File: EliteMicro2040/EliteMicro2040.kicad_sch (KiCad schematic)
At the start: 40 parts, among them J2 Button, J5 Conn_01x03_Male, U101 TLV70033, U2 Elite-C, U3 RP2040, Y1 2520_4P 12Mhz

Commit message: preparation for order.
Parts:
- removed J5: Conn_01x03_Male, Connector_PinHeader_2.54mm:PinHeader_1x03_P2.54mm_Vertical, symbol Connector_Generic:Conn_01x03
- added TP101, TP102, TP103: TestPoint, EnvExtras:CustomTestPoint, symbol Connector:TestPoint
- FLASH1: value W25Q16FWUXIE -> W25Q16JVUXIQ
- USB1: LCSC C165948 -> C223907
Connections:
- net GND: now also TP102.1
- net SWCLK: now also TP101.1
- net SWD: now also TP103.1
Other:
- note removed: "D1 NEEDS to be 0omh resistor or 1N4002 diode"
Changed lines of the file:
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@@
     (effects (font (size 1.27 1.27)) (justify right bottom))
-  )
-  (text "D1 NEEDS to be 0omh resistor or 1N4002 diode" (at 70.485 47.625 0)
-    (effects (font (size 0.508 0.508)) (justify left bottom))
   )
   (text "Im pretty sure a lot of these W25QXXX Chips are pin compatible\nDont quote me on that"
@@
       (effects (font (size 1.27 1.27)) hide)
     )
-    (property "LCSC" "C165948" (id 4) (at 25.4 35.56 0)
+    (property "LCSC" "C223907" (id 4) (at 25.4 35.56 0)
       (effects (font (size 1.27 1.27)) hide)
     )
@@
     (in_bom yes) (on_board yes)
     (property "Reference" "FLASH1" (id 0) (at 78.74 133.35 0))
-    (property "Value" "W25Q16FWUXIE" (id 1) (at 78.74 146.05 0))
+    (property "Value" "W25Q16JVUXIQ" (id 1) (at 78.74 146.05 0))
     (property "Footprint" "Package_SON:SON-8-1EP_3x2mm_P0.5mm_EP1.4x1.6mm" (id 2) (at 78.74 133.35 0)
       (effects (font (size 1.27 1.27)) (justify left bottom) hide)
@@
     )
     (pin "1")
-  )
-  (symbol (lib_id "Connector_Generic:Conn_01x03") (at 375.92 177.8 0) (unit 1)
-    (in_bom yes) (on_board yes)
-    (property "Reference" "J5" (id 0) (at 377.952 176.7332 0)
-      (effects (font (size 1.27 1.27)) (justify left))
-    )
-    (property "Value" "Conn_01x03_Male" (id 1) (at 377.952 179.0446 0)
-      (effects (font (size 1.27 1.27)) (justify left))
-    )
-    (property "Footprint" "Connector_PinHeader_2.54mm:PinHeader_1x03_P2.54mm_Vertical" (id 2) (at 375.92 177.8 0)
-      (effects (font (size 1.27 1.27)) hide)
-    )
-    (property "Datasheet" "" (id 3) (at 375.92 177.8 0)
-      (effects (font (size 1.27 1.27)) hide)
-    )
-    (property "LCSC" " " (id 4) (at 375.92 177.8 0)
-      (effects (font (size 1.27 1.27)) hide)
-    )
-    (pin "1")
-    (pin "2")
-    (pin "3")
   )
   (symbol (lib_id "power:GND") (at 370.84 177.8 270) (unit 1)
@@
     (pin "1")
   )
+  (symbol (lib_id "Connector:TestPoint") (at 370.84 177.8 270) (unit 1)
+    (in_bom yes) (on_board yes)
+    (property "Reference" "TP102" (id 0) (at 375.6152 177.2412 90)
+      (effects (font (size 0.508 0.508)) (justify left))
+    )
+    (property "Value" "TestPoint" (id 1) (at 375.6152 178.3334 90)
+      (effects (font (size 0.508 0.508)) (justify left))
+    )
+    (property "Footprint" "EnvExtras:CustomTestPoint" (id 2) (at 370.84 182.88 0)
+      (effects (font (size 1.27 1.27)) hide)
+    )
+    (property "Datasheet" "" (id 3) (at 370.84 182.88 0)
+      (effects (font (size 1.27 1.27)) hide)
+    )
+    (property "LCSC" " " (id 4) (at 370.84 177.8 0)
+      (effects (font (size 1.27 1.27)) hide)
+    )
+    (pin "1")
+  )
   (symbol (lib_id "power:GND") (at 68.58 57.15 0) (unit 1)
     (in_bom yes) (on_board yes)
@@
     (pin "1")
     (pin "2")
+  )
+  (symbol (lib_id "Connector:TestPoint") (at 370.84 175.26 270) (unit 1)
+    (in_bom yes) (on_board yes)
+    (property "Reference" "TP101" (id 0) (at 375.6152 174.7012 90)
+      (effects (font (size 0.508 0.508)) (justify left))
+    )
+    (property "Value" "TestPoint" (id 1) (at 375.6152 175.7934 90)
+      (effects (font (size 0.508 0.508)) (justify left))
+    )
+    (property "Footprint" "EnvExtras:CustomTestPoint" (id 2) (at 370.84 180.34 0)
+      (effects (font (size 1.27 1.27)) hide)
+    )
+    (property "Datasheet" "" (id 3) (at 370.84 180.34 0)
+      (effects (font (size 1.27 1.27)) hide)
+    )
+    (property "LCSC" " " (id 4) (at 370.84 175.26 0)
+      (effects (font (size 1.27 1.27)) hide)
+    )
+    (pin "1")
+  )
+  (symbol (lib_id "Connector:TestPoint") (at 370.84 180.34 270) (unit 1)
+    (in_bom yes) (on_board yes)
+    (property "Reference" "TP103" (id 0) (at 375.6152 179.7812 90)
+      (effects (font (size 0.508 0.508)) (justify left))
+    )
+    (property "Value" "TestPoint" (id 1) (at 375.6152 180.8734 90)
+      (effects (font (size 0.508 0.508)) (justify left))
+    )
+    (property "Footprint" "EnvExtras:CustomTestPoint" (id 2) (at 370.84 185.42 0)
+      (effects (font (size 1.27 1.27)) hide)
+    )
+    (property "Datasheet" "" (id 3) (at 370.84 185.42 0)
+      (effects (font (size 1.27 1.27)) hide)
+    )
+    (property "LCSC" " " (id 4) (at 370.84 180.34 0)
+      (effects (font (size 1.27 1.27)) hide)
+    )
+    (pin "1")
   )
   (sheet_instances
@@
     )
     (path "/00000000-0000-0000-0000-0000608edada"
-      (reference "FLASH1") (unit 1) (value "W25Q16FWUXIE") (footprint "Package_SON:SON-8-1EP_3x2mm_P0.5mm_EP1.4x1.6mm")
+      (reference "FLASH1") (unit 1) (value "W25Q16JVUXIQ") (footprint "Package_SON:SON-8-1EP_3x2mm_P0.5mm_EP1.4x1.6mm")
     )
     (path "/00000000-0000-0000-0000-000060cc7b32"
@@
       (reference "J2") (unit 1) (value "Button") (footprint "Button_Switch_SMD:SW_SPST_CK_KXT3")
     )
-    (path "/00000000-0000-0000-0000-000060ce2dd4"
-      (reference "J5") (unit 1) (value "Conn_01x03_Male") (footprint "Connector_PinHeader_2.54mm:PinHeader_1x03_P2.54mm_Vertical")
-    )
     (path "/00000000-0000-0000-0000-00005edae9f0"
       (reference "R1") (unit 1) (value "1K 402 Resistor") (footprint "Capacitor_SMD:C_0402_1005Metric")
@@
       (reference "TP4") (unit 1) (value "TestPoint") (footprint "EnvExtras:CustomTestPoint")
     )
+    (path "/cc629fb9-56a0-47df-8b5b-822906a0848a"
+      (reference "TP101") (unit 1) (value "TestPoint") (footprint "EnvExtras:CustomTestPoint")
+    )
+    (path "/42a77294-7232-471b-9aeb-b80d6a159af4"
+      (reference "TP102") (unit 1) (value "TestPoint") (footprint "EnvExtras:CustomTestPoint")
+    )
+    (path "/e62dbc5e-8e6b-40c9-9254-b5ec34005539"
+      (reference "TP103") (unit 1) (value "TestPoint") (footprint "EnvExtras:CustomTestPoint")
+    )
     (path "/00000000-0000-0000-0000-000061b490e3"

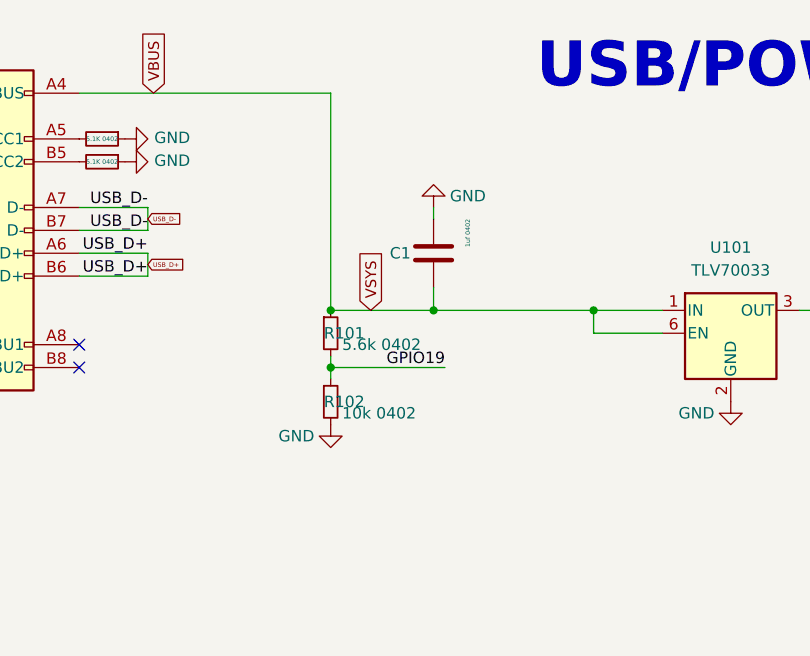
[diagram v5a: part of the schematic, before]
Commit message: added diode after VBUS to make sure VBUS Detect can work properly.
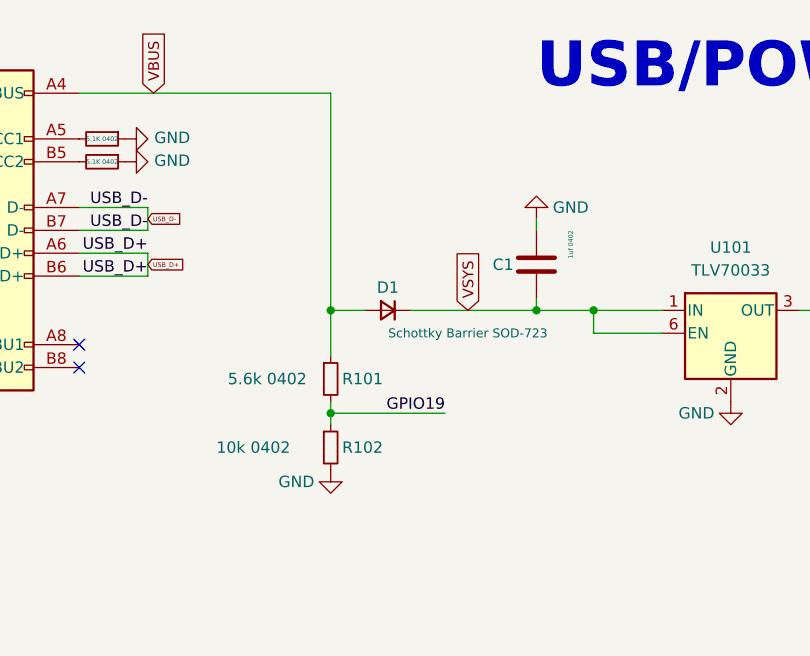
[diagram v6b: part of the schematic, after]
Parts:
- added D1: Schottky Barrier SOD-723, Diode_SMD:D_SOD-523, symbol Device:D_Small
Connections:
- net VBUS: now also D1.2 (A); no longer C1.1, U101.1 (IN), U101.6 (EN)
- new net VSYS: C1.1, D1.1 (K), U101.1 (IN), U101.6 (EN)
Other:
- moved on the sheet: C1, R101, R102

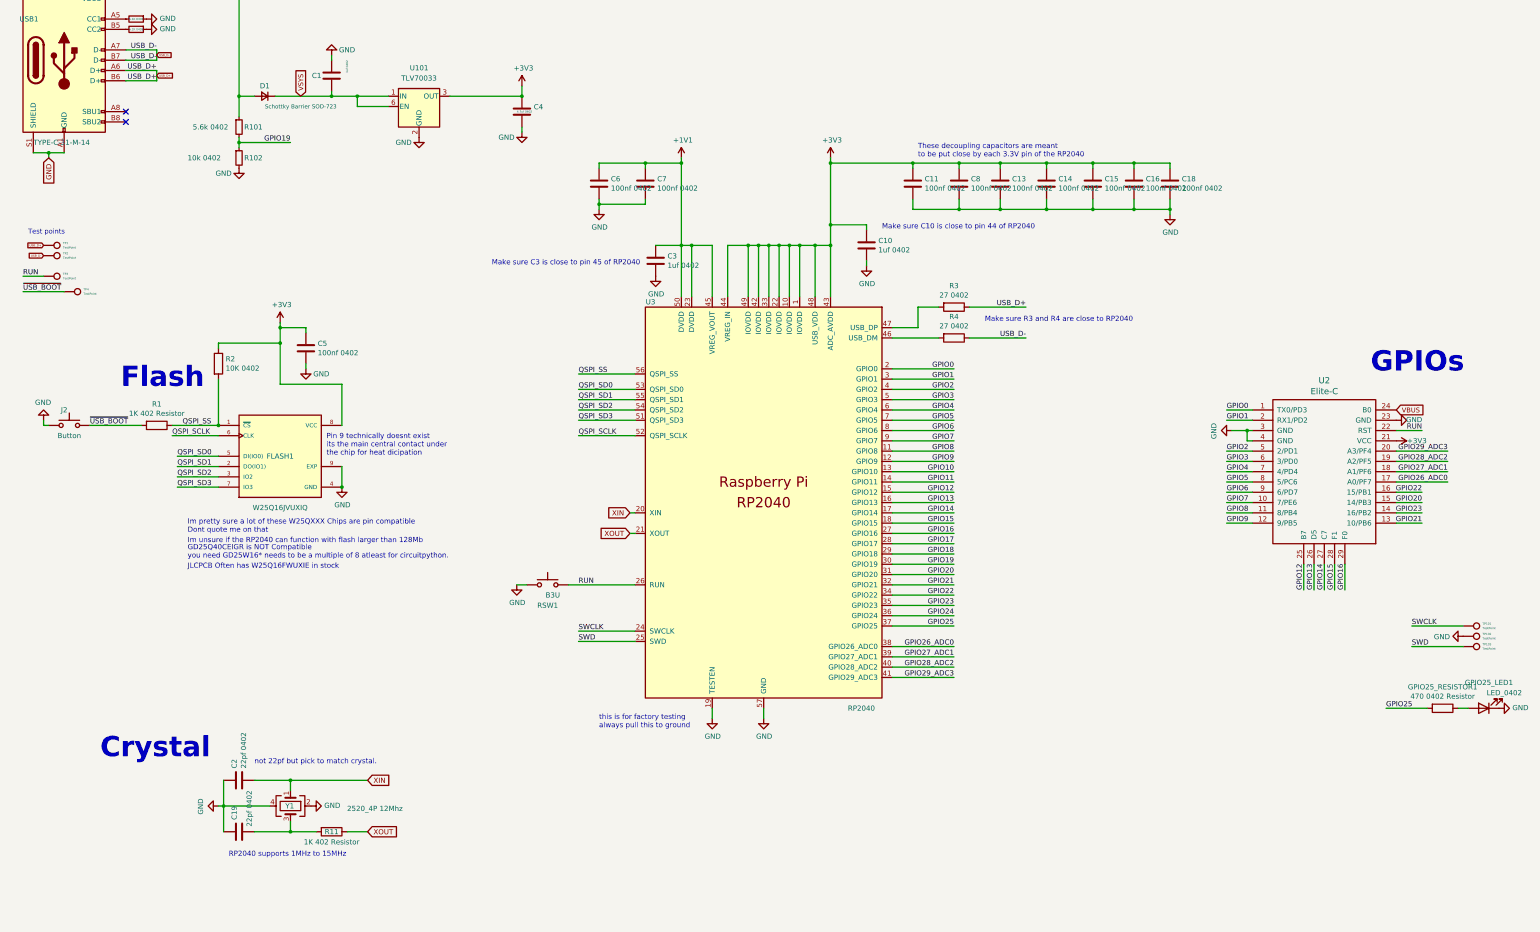
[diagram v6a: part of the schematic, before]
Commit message: made various improvements to design such as swapping vbus for vsys on the raw pin
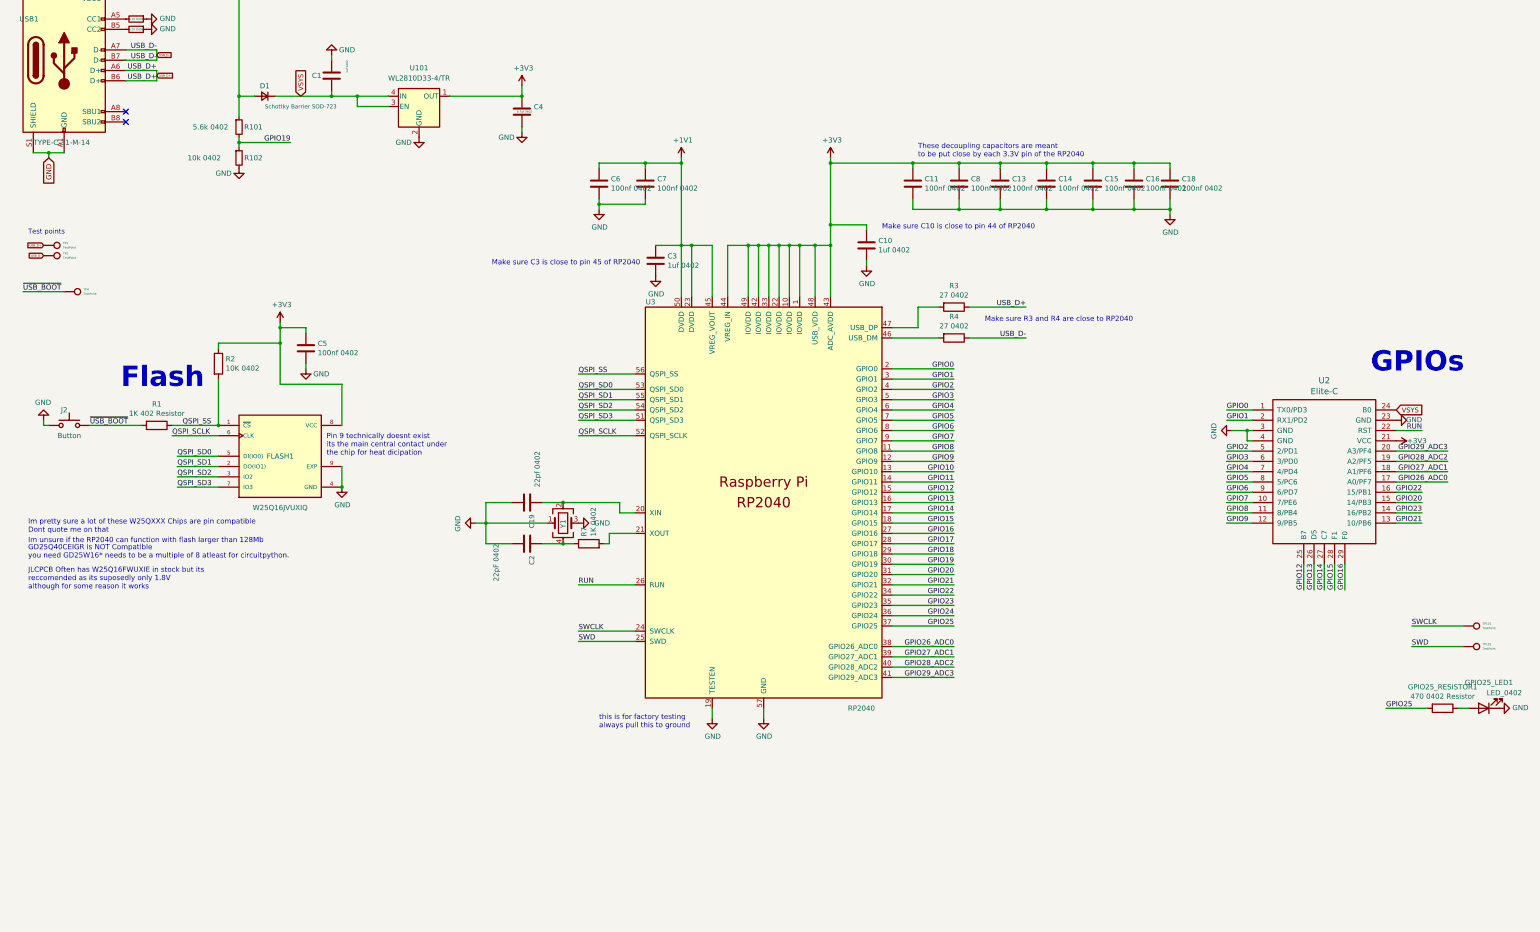
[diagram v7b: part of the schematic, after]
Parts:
- removed R11: 1K 402 Resistor, Capacitor_SMD:C_0402_1005Metric, symbol Device:R
- removed RSW1: B3U, Button_Switch_SMD:SW_SPST_B3U-1000P, symbol Switch:SW_Push
- removed TP102, TP3: TestPoint, EnvExtras:CustomTestPoint, symbol Connector:TestPoint
- added R7: 1K 0402, Capacitor_SMD:C_0402_1005Metric, symbol Device:R
- C2: value 22pf 0402 -> 22pF 0402
- U101: value TLV70033 -> WL2810D33-4/TR; footprint Package_SON:WSON-6_1.5x1.5mm_P0.5mm -> Package_DFN_QFN:UDFN-4-1EP_1x1mm_P0.65mm_EP0.48x0.48mm
- Y1: value 2520_4P 12Mhz -> 2016_4P; footprint Crystal:Crystal_SMD_2520-4Pin_2.5x2.0mm -> Crystal:Crystal_SMD_2016-4Pin_2.0x1.6mm
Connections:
- net +3V3: now also U101.1 (OUT); no longer U101.3 (OUT)
- net GND: now also C19.2, C2.2, Y1.1, Y1.3; no longer C19.1, C2.1, Y1.2, Y1.4
- net VBUS: no longer U2.24 (B0)
- net VSYS: now also U101.3 (EN), U101.4 (NC), U2.24 (B0); no longer U101.1 (IN), U101.6 (EN)
- removed net XIN: C2.2, U3.20 (XIN), Y1.1
- net XOUT: no longer names the net of U3.21 (XOUT)
- net XOUT: now also R7.2
- new net: C19.1, U3.20 (XIN), Y1.2
- new net: C2.1, R7.1, Y1.4
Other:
- note added: "JLCPCB Often has W25Q16FWUXIE in stock but its reccomended as its suposedly only 1.8V although for some reason it works"
- note removed: "Crystal"
- note removed: "JLCPCB Often has W25Q16FWUXIE in stock"
- note removed: "RP2040 supports 1MHz to 15MHz"
- note removed: "not 22pf but pick to match crystal."
- moved on the sheet: C19, C2, Y1

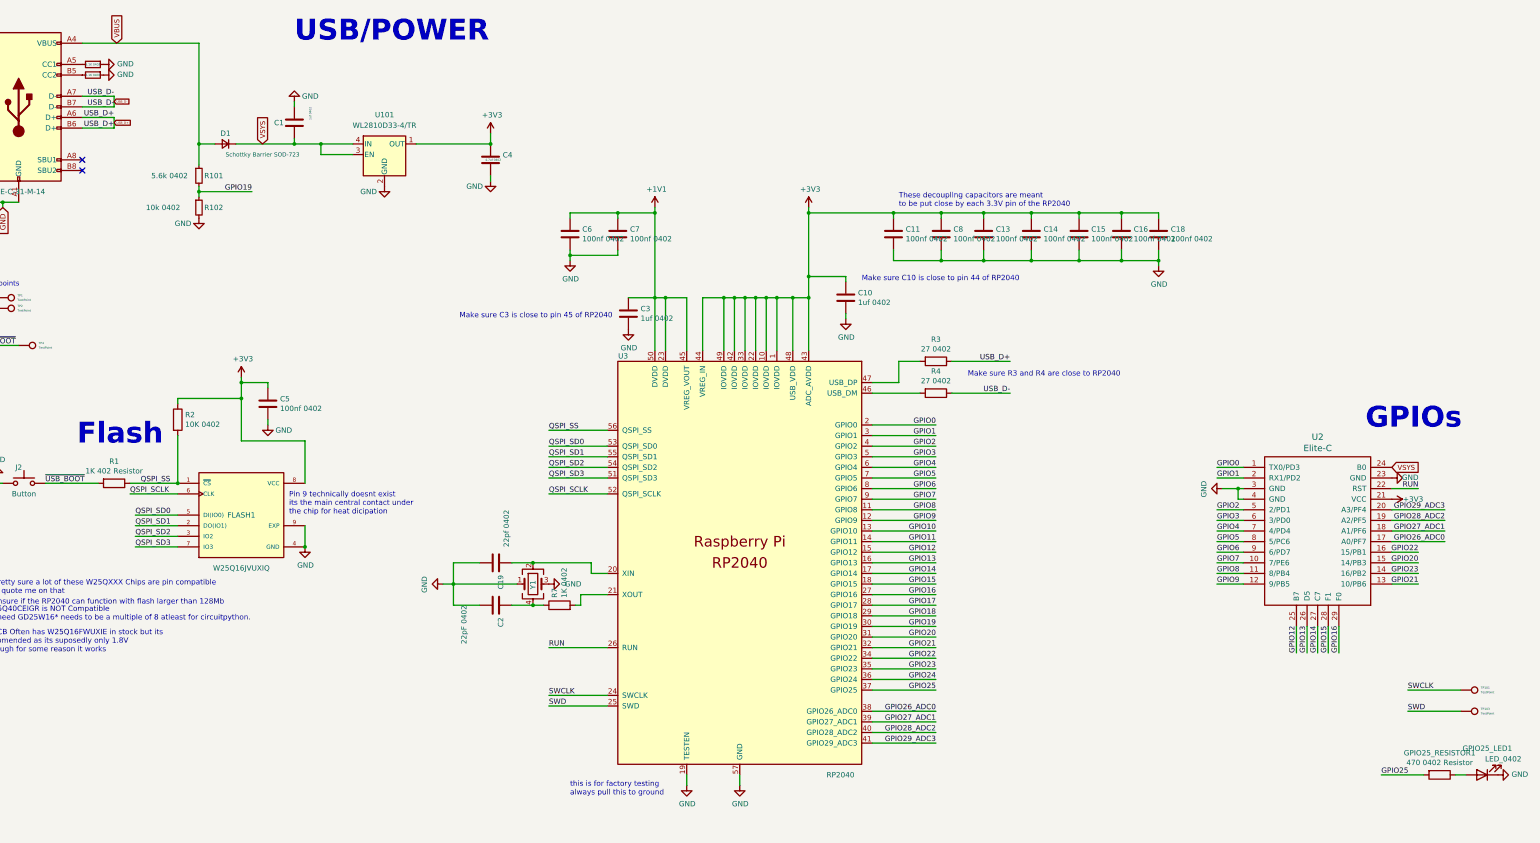
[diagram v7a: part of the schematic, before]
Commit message: General re-work of board to ensure less chance of failure
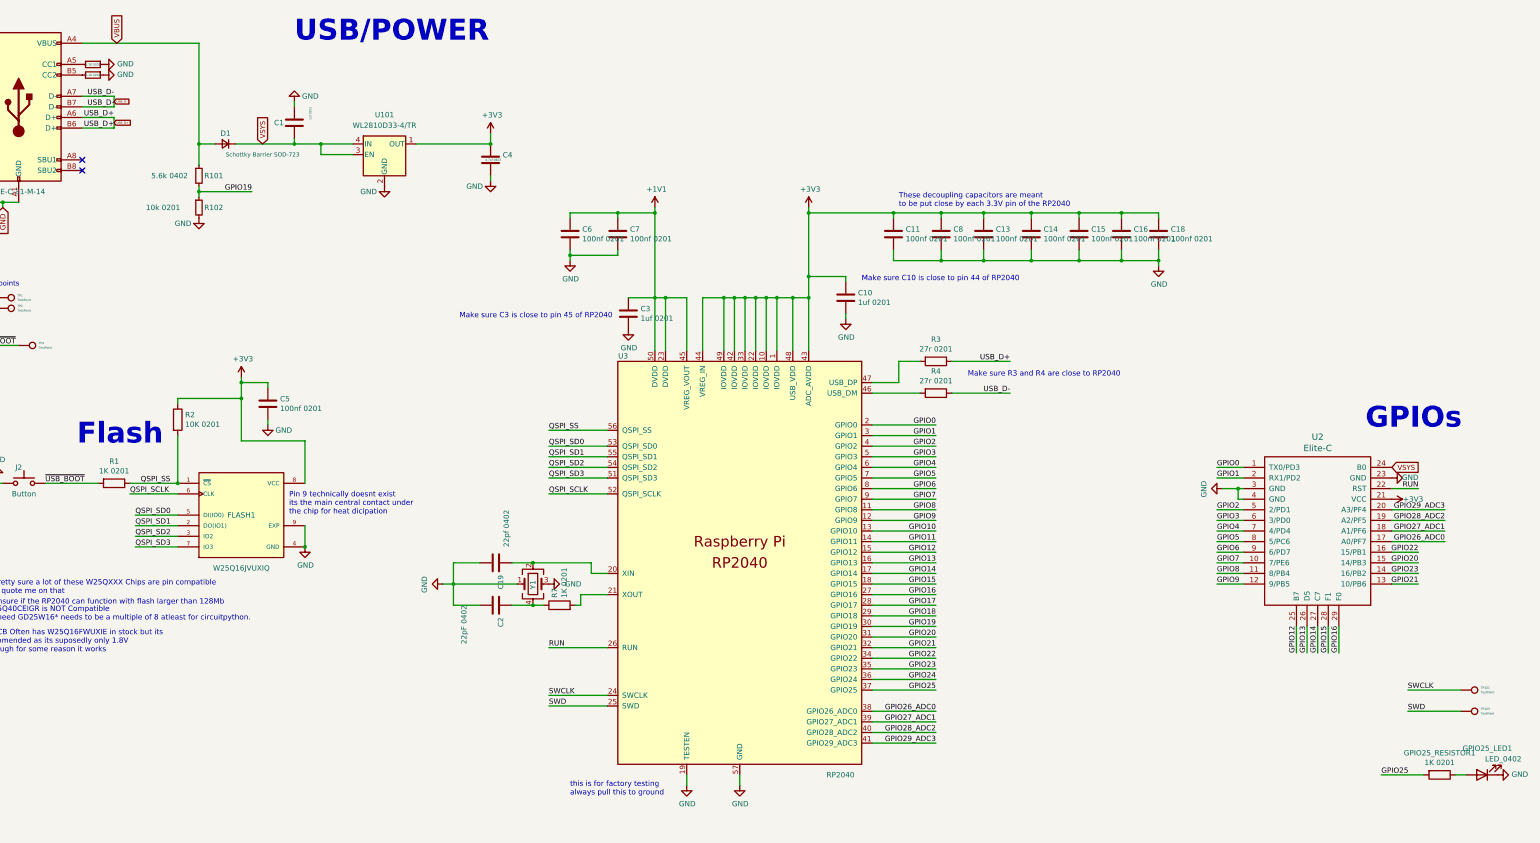
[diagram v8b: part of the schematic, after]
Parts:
- C1, C10, C3: value 1uf 0402 -> 1uf 0201; footprint Capacitor_SMD:C_0402_1005Metric -> Capacitor_SMD:C_0201_0603Metric
- C11, C13, C14, C15, C16, C18, C5, C6, C7, C8: value 100nf 0402 -> 100nf 0201; footprint Capacitor_SMD:C_0402_1005Metric -> Capacitor_SMD:C_0201_0603Metric
- GPIO25_RESISTOR1: value 470 0402 Resistor -> 1K 0201; footprint Resistor_SMD:R_0402_1005Metric -> Resistor_SMD:R_0201_0603Metric
- R1: value 1K 402 Resistor -> 1K 0201; footprint Capacitor_SMD:C_0402_1005Metric -> Capacitor_SMD:C_0201_0603Metric
- R102: value 10k 0402 -> 10k 0201; footprint Resistor_SMD:R_0402_1005Metric -> Resistor_SMD:R_0201_0603Metric
- R2: value 10K 0402 -> 10K 0201; footprint Capacitor_SMD:C_0402_1005Metric -> Capacitor_SMD:C_0201_0603Metric
- R3, R4: value 27 0402 -> 27r 0201; footprint Resistor_SMD:R_0402_1005Metric -> Resistor_SMD:R_0201_0603Metric
- R5, R6: value 5.1K 0402 -> 5.1K 0201; footprint Resistor_SMD:R_0402_1005Metric -> Resistor_SMD:R_0201_0603Metric
- R7: value 1K 0402 -> 1K 0201; footprint Capacitor_SMD:C_0402_1005Metric -> Capacitor_SMD:C_0201_0603Metric
